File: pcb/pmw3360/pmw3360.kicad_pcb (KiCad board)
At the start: 2 copper layers, 25 x 30 mm, 20 parts, among them J1 Connector, J2 PinOut, U1 PMW3360DM-T2QU, U2 TCR2EF19,LM(CT, U3 SN74LVC1T45QDCKRQ1, U4 TXB0104RUT

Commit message: change route
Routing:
- net Net-(R1-Pad1): track 28.7 -> 27.8 mm
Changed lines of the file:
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@@
   (via (at 100.9 101.3) (size 0.8) (drill 0.4) (layers F.Cu B.Cu) (net 13))
   (segment (start 101.125645 97.974355) (end 101.125645 97.949487) (width 0.25) (layer F.Cu) (net 13))
+  (segment (start 113.025 98.575) (end 115.4 96.2) (width 0.25) (layer B.Cu) (net 13))
+  (segment (start 100.9 101.3) (end 100.9 103) (width 0.25) (layer B.Cu) (net 13))
   (segment (start 100.9 103) (end 102 104.1) (width 0.25) (layer B.Cu) (net 13))
-  (segment (start 100.9 101.3) (end 100.9 103) (width 0.25) (layer B.Cu) (net 13))
-  (segment (start 115 101.7) (end 115 96.6) (width 0.25) (layer B.Cu) (net 13))
-  (segment (start 102 104.1) (end 112.6 104.1) (width 0.25) (layer B.Cu) (net 13))
-  (segment (start 115 96.6) (end 115.4 96.2) (width 0.25) (layer B.Cu) (net 13))
-  (segment (start 112.6 104.1) (end 115 101.7) (width 0.25) (layer B.Cu) (net 13))
+  (segment (start 102 104.1) (end 111 104.1) (width 0.25) (layer B.Cu) (net 13))
+  (segment (start 111 104.1) (end 113.025 102.075) (width 0.25) (layer B.Cu) (net 13))
+  (segment (start 113.025 102.075) (end 113.025 98.575) (width 0.25) (layer B.Cu) (net 13))
   (segment (start 99.6 85.2) (end 99.6 92.863842) (width 0.25) (layer F.Cu) (net 14))
   (segment (start 99.6 92.863842) (end 101.125645 94.389487) (width 0.25) (layer F.Cu) (net 14))

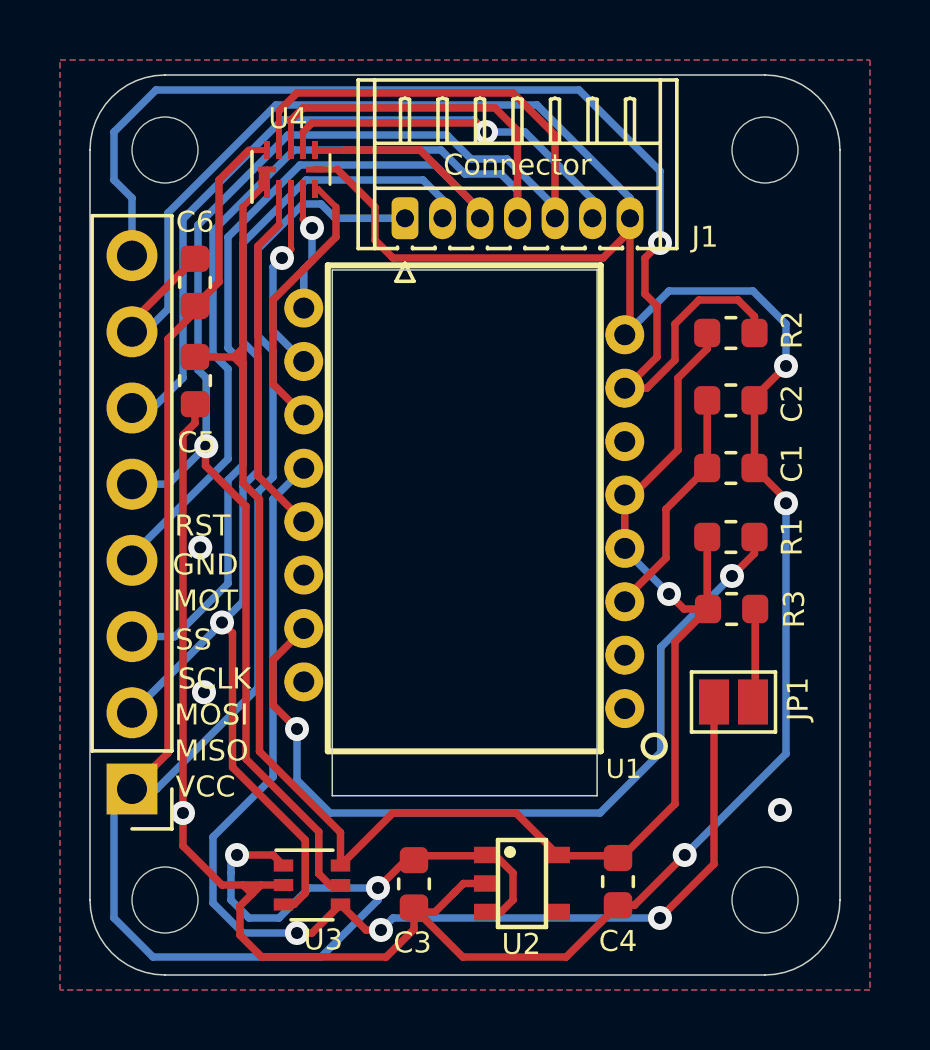
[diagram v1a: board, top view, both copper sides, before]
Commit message: change footprints position
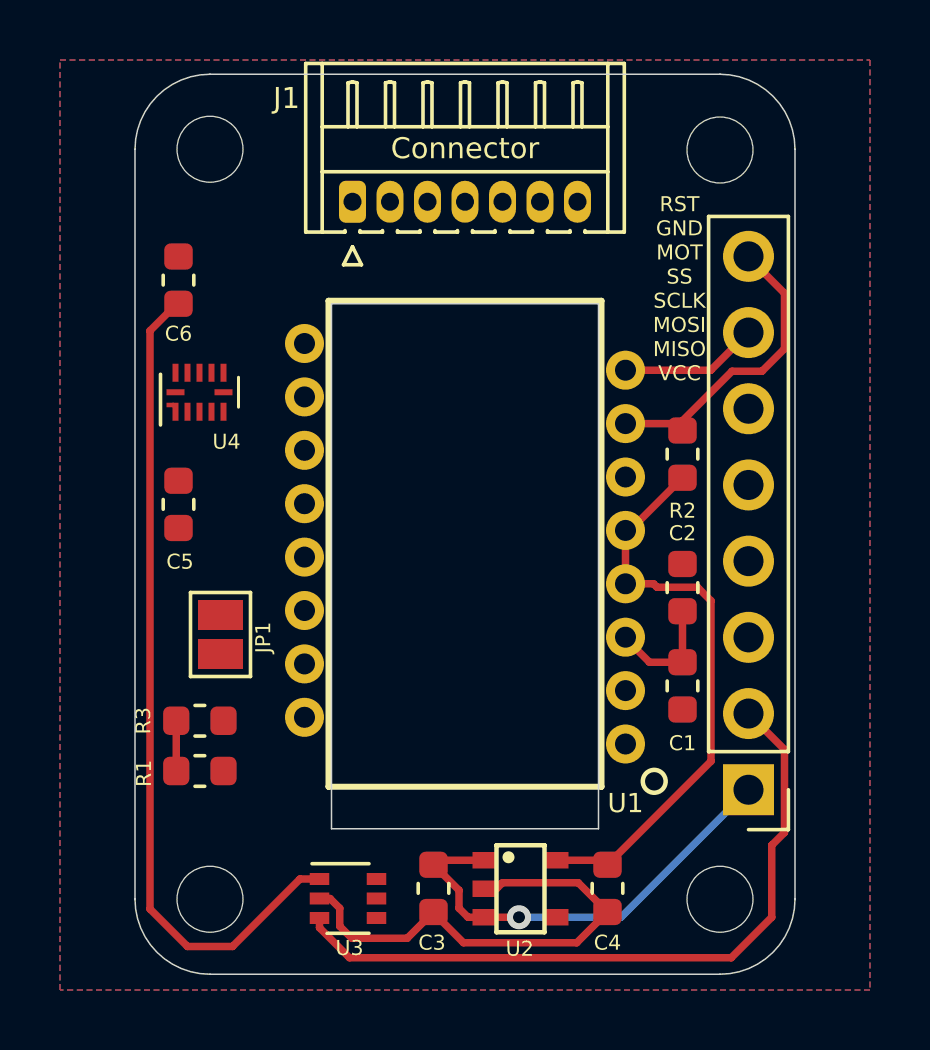
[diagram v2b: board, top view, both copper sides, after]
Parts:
- removed the REF** at (116.5, 107.0)
- removed the REF** at (96.5, 82.0)
- removed the REF** at (116.5, 82.0)
- added REF**: MountingHole_2.2mm_M2, MountingHole:MountingHole_2.2mm_M2, F.Cu at (115.0, 107.0)
- added REF**: MountingHole_2.2mm_M2, MountingHole:MountingHole_2.2mm_M2, F.Cu at (98.0, 82.0)
- added REF**: MountingHole_2.2mm_M2, MountingHole:MountingHole_2.2mm_M2, F.Cu at (115.0, 82.0)
- moved J2 20.6 mm to (116.0, 103.3)
- moved R1 19.3 mm to (97.7, 102.7)
- moved R3 18.1 mm to (97.7, 101.0)
- moved JP1 17.2 mm to (98.3, 98.2), turned to 270 degrees
- moved U4 8.03 mm to (97.7, 90.1)
- moved C1 7.44 mm to (113.8, 99.9), turned to 270 degrees
- moved C2 6.45 mm to (113.8, 96.6), turned to 90 degrees
- moved R2 4.35 mm to (113.8, 92.1), turned to 90 degrees
- moved C5 4.16 mm to (97.0, 93.8)
- moved J1 1.83 mm to (102.8, 83.7)
- moved REF** 1.50 mm to (98.0, 107.0)
- moved U3 1.28 mm to (102.6, 107.0)
- moved U1 1.18 mm to (106.5, 95.1)
- moved C3 0.67 mm to (105.5, 106.6)
- moved C6 0.56 mm to (97.0, 86.3)
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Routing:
- net GND: track 113.3 -> 20.9 mm, vias 7 -> 0
- net /SS-H: track 56.5 -> 0.00 mm, vias 1 -> 0
- net VDD: track 62.8 -> 21.2 mm, vias 1 -> 0
- net /MISO: track 39.9 -> 0.00 mm, vias 3 -> 0
- net VCC: track 81.0 -> 42.8 mm, vias 2 -> 1
- net /SCLK-H: track 37.2 -> 0.00 mm
- net /MOSI-H: track 32.8 -> 0.00 mm
- net /MOT-H: track 31.1 -> 0.00 mm, vias 1 -> 0
- net /NRESET: track 39.4 -> 10.3 mm, vias 1 -> 0
- net Net-(R1-Pad1): track 27.8 -> 0.00 mm, vias 2 -> 0
- net /MISO-H: track 37.1 -> 23.8 mm, vias 1 -> 0
- net /SS: track 12.0 -> 0.00 mm
- net /MOSI: track 9.17 -> 0.00 mm
- net /SCLK: track 6.42 -> 0.00 mm, vias 1 -> 0
- net /MOT: track 4.21 -> 0.00 mm, vias 1 -> 0
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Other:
- board size 25 x 30 mm -> 22 x 30 mm
- board text added: "RST GND MOT SS SCLK MOSI MISO VCC"
- board text removed: "GND"
- board text removed: "MISO"
- board text removed: "MOSI"
- board text removed: "MOT"
- board text removed: "RST"
- board text removed: "SCLK"
- board text removed: "SS"
- board text removed: "VCC"

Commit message: Change U3 position
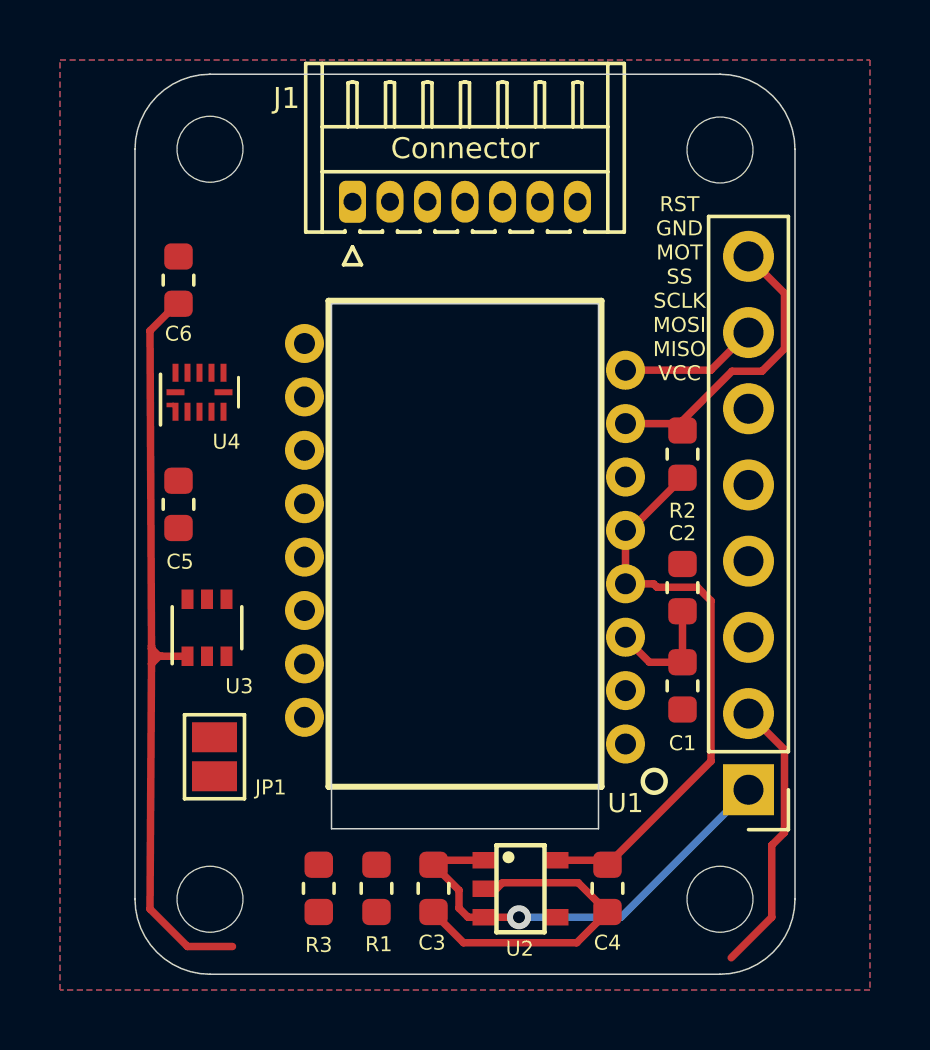
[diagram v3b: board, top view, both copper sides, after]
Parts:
- moved U3 10.2 mm to (97.9, 97.9), turned to 90 degrees
- moved R1 7.07 mm to (103.5, 106.6), turned to 270 degrees
- moved R3 6.85 mm to (101.6, 106.6), turned to 90 degrees
- moved JP1 4.08 mm to (98.2, 102.2)
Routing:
- net /MISO-H: track 23.8 -> 9.37 mm
- net GND: track 20.9 -> 15.9 mm
- net VCC: track 42.8 -> 40.7 mm
- net VDD: track 21.2 -> 19.5 mm
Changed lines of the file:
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@@
     (thickness 1.6)
     (drawings 15)
-    (tracks 66)
+    (tracks 61)
     (zones 0)
     (modules 20)
@@
   )
   (module Resistor_SMD:R_0603_1608Metric (layer F.Cu)
-    (at 97.6625 102.7 180)
+    (at 103.55 106.6125 270)
     (descr "Resistor SMD 0603 (1608 Metric), square (rectangular) end terminal, IPC_7351 nominal, (Body size source: http://www.tortai-tech.com/upload/download/2011102023233369053.pdf), generated with kicad-footprint-generator")
     (tags resistor)
     (attr smd)
-    (fp_text reference R1 (at 1.8625 -0.075 90) (layer F.SilkS)
-      (effects (font (size 0.5 0.5) (thickness 0.1)))
-    )
-    (fp_text value 39R (at -1.8375 0.025 90) (layer F.Fab)
-      (effects (font (size 0.5 0.5) (thickness 0.1)))
-    )
-    (fp_text user %R (at 0 0) (layer F.Fab)
+    (fp_text reference R1 (at 1.8625 -0.075) (layer F.SilkS)
+      (effects (font (size 0.5 0.5) (thickness 0.1)))
+    )
+    (fp_text value 39R (at 2.4875 -0.05) (layer F.Fab)
+      (effects (font (size 0.5 0.5) (thickness 0.1)))
+    )
+    (fp_text user %R (at 0 0 90) (layer F.Fab)
       (effects (font (size 0.4 0.4) (thickness 0.06)))
     )
@@
     (fp_line (start -0.8 -0.4) (end 0.8 -0.4) (layer F.Fab) (width 0.1))
     (fp_line (start -0.8 0.4) (end -0.8 -0.4) (layer F.Fab) (width 0.1))
-    (pad 2 smd roundrect (at 0.7875 0 180) (size 0.875 0.95) (layers F.Cu F.Paste F.Mask) (roundrect_rratio 0.25)
-      (net 4 VDD))
-    (pad 1 smd roundrect (at -0.7875 0 180) (size 0.875 0.95) (layers F.Cu F.Paste F.Mask) (roundrect_rratio 0.25)
+    (pad 2 smd roundrect (at 0.7875 0 270) (size 0.875 0.95) (layers F.Cu F.Paste F.Mask) (roundrect_rratio 0.25)
+      (net 4 VDD))
+    (pad 1 smd roundrect (at -0.7875 0 270) (size 0.875 0.95) (layers F.Cu F.Paste F.Mask) (roundrect_rratio 0.25)
       (net 13 "Net-(R1-Pad1)"))
     (model ${KISYS3DMOD}/Resistor_SMD.3dshapes/R_0603_1608Metric.wrl
@@
   )
   (module Resistor_SMD:R_0603_1608Metric (layer F.Cu)
-    (at 97.6625 101.025)
+    (at 101.625 106.6125 90)
     (descr "Resistor SMD 0603 (1608 Metric), square (rectangular) end terminal, IPC_7351 nominal, (Body size source: http://www.tortai-tech.com/upload/download/2011102023233369053.pdf), generated with kicad-footprint-generator")
     (tags resistor)
     (attr smd)
-    (fp_text reference R3 (at -1.8875 0 90) (layer F.SilkS)
-      (effects (font (size 0.5 0.5) (thickness 0.1)))
-    )
-    (fp_text value 10k (at 1.8125 0 90) (layer F.Fab)
-      (effects (font (size 0.5 0.5) (thickness 0.1)))
-    )
-    (fp_text user %R (at 0 0) (layer F.Fab)
+    (fp_text reference R3 (at -1.8875 0) (layer F.SilkS)
+      (effects (font (size 0.5 0.5) (thickness 0.1)))
+    )
+    (fp_text value 10k (at -2.5375 0) (layer F.Fab)
+      (effects (font (size 0.5 0.5) (thickness 0.1)))
+    )
+    (fp_text user %R (at 0 0 90) (layer F.Fab)
       (effects (font (size 0.4 0.4) (thickness 0.06)))
     )
@@
     (fp_line (start -0.8 -0.4) (end 0.8 -0.4) (layer F.Fab) (width 0.1))
     (fp_line (start -0.8 0.4) (end -0.8 -0.4) (layer F.Fab) (width 0.1))
-    (pad 2 smd roundrect (at 0.7875 0) (size 0.875 0.95) (layers F.Cu F.Paste F.Mask) (roundrect_rratio 0.25)
+    (pad 2 smd roundrect (at 0.7875 0 90) (size 0.875 0.95) (layers F.Cu F.Paste F.Mask) (roundrect_rratio 0.25)
       (net 12 "Net-(JP1-Pad2)"))
-    (pad 1 smd roundrect (at -0.7875 0) (size 0.875 0.95) (layers F.Cu F.Paste F.Mask) (roundrect_rratio 0.25)
+    (pad 1 smd roundrect (at -0.7875 0 90) (size 0.875 0.95) (layers F.Cu F.Paste F.Mask) (roundrect_rratio 0.25)
       (net 4 VDD))
     (model ${KISYS3DMOD}/Resistor_SMD.3dshapes/R_0603_1608Metric.wrl
@@
   )
   (module Package_TO_SOT_SMD:SOT-363_SC-70-6 (layer F.Cu)
-    (at 102.6 106.95)
+    (at 97.9 97.925 90)
     (descr "SOT-363, SC-70-6")
     (tags "SOT-363 SC-70-6")
     (attr smd)
-    (fp_text reference U3 (at 0.05 1.65) (layer F.SilkS)
-      (effects (font (size 0.5 0.5) (thickness 0.1)))
-    )
-    (fp_text value SN74LVC1T45QDCKRQ1 (at -0.15 6.625 -270) (layer F.Fab)
+    (fp_text reference U3 (at -1.95 1.075 180) (layer F.SilkS)
+      (effects (font (size 0.5 0.5) (thickness 0.1)))
+    )
+    (fp_text value SN74LVC1T45QDCKRQ1 (at -0.15 6.625) (layer F.Fab)
       (effects (font (size 0.5 0.5) (thickness 0.1)))
     )
@@
     (fp_line (start -0.7 1.16) (end 0.7 1.16) (layer F.SilkS) (width 0.12))
     (fp_line (start 0.7 -1.16) (end -1.2 -1.16) (layer F.SilkS) (width 0.12))
-    (fp_text user %R (at 0 0 -270) (layer F.Fab)
+    (fp_text user %R (at 0 0) (layer F.Fab)
       (effects (font (size 0.5 0.5) (thickness 0.075)))
     )
-    (pad 6 smd rect (at 0.95 -0.65) (size 0.65 0.4) (layers F.Cu F.Paste F.Mask)
-      (net 4 VDD))
-    (pad 4 smd rect (at 0.95 0.65) (size 0.65 0.4) (layers F.Cu F.Paste F.Mask)
+    (pad 6 smd rect (at 0.95 -0.65 90) (size 0.65 0.4) (layers F.Cu F.Paste F.Mask)
+      (net 4 VDD))
+    (pad 4 smd rect (at 0.95 0.65 90) (size 0.65 0.4) (layers F.Cu F.Paste F.Mask)
       (net 11 /MISO))
-    (pad 2 smd rect (at -0.95 0) (size 0.65 0.4) (layers F.Cu F.Paste F.Mask)
-      (net 1 GND))
-    (pad 5 smd rect (at 0.95 0) (size 0.65 0.4) (layers F.Cu F.Paste F.Mask)
+    (pad 2 smd rect (at -0.95 0 90) (size 0.65 0.4) (layers F.Cu F.Paste F.Mask)
+      (net 1 GND))
+    (pad 5 smd rect (at 0.95 0 90) (size 0.65 0.4) (layers F.Cu F.Paste F.Mask)
       (net 6 /SS-H))
-    (pad 3 smd rect (at -0.95 0.65) (size 0.65 0.4) (layers F.Cu F.Paste F.Mask)
+    (pad 3 smd rect (at -0.95 0.65 90) (size 0.65 0.4) (layers F.Cu F.Paste F.Mask)
       (net 9 /MISO-H))
-    (pad 1 smd rect (at -0.95 -0.65) (size 0.65 0.4) (layers F.Cu F.Paste F.Mask)
+    (pad 1 smd rect (at -0.95 -0.65 90) (size 0.65 0.4) (layers F.Cu F.Paste F.Mask)
       (net 3 VCC))
     (model ${KISYS3DMOD}/Package_TO_SOT_SMD.3dshapes/SOT-363_SC-70-6.wrl
@@
   )
   (module Jumper:SolderJumper-2_P1.3mm_Open_Pad1.0x1.5mm (layer F.Cu)
-    (at 98.35 98.15 270)
+    (at 98.15 102.225 270)
     (descr "SMD Solder Jumper, 1x1.5mm Pads, 0.3mm gap, open")
     (tags "solder jumper open")
     (attr virtual)
-    (fp_text reference JP1 (at 0.1 -1.425 90) (layer F.SilkS)
-      (effects (font (size 0.5 0.5) (thickness 0.1)))
-    )
-    (fp_text value JP_Open (at 5.725 -0.2 90) (layer F.Fab)
+    (fp_text reference JP1 (at 1.025 -1.875 180) (layer F.SilkS)
+      (effects (font (size 0.5 0.5) (thickness 0.1)))
+    )
+    (fp_text value JP_Open (at -1.375 15.45 90) (layer F.Fab)
       (effects (font (size 1 1) (thickness 0.15)))
     )
@@
   (segment (start 106.45 108.425) (end 110.225 108.425) (width 0.25) (layer F.Cu) (net 1))
   (segment (start 105.45 107.425) (end 106.45 108.425) (width 0.25) (layer F.Cu) (net 1))
-  (segment (start 104.575 108.275) (end 105.45 107.4) (width 0.25) (layer F.Cu) (net 1))
-  (segment (start 101.65 106.95) (end 102 106.95) (width 0.25) (layer F.Cu) (net 1))
-  (segment (start 102 106.95) (end 102.325 107.275) (width 0.25) (layer F.Cu) (net 1))
-  (segment (start 102.325 107.875) (end 102.725 108.275) (width 0.25) (layer F.Cu) (net 1))
-  (segment (start 102.325 107.275) (end 102.325 107.875) (width 0.25) (layer F.Cu) (net 1))
-  (segment (start 102.725 108.275) (end 104.575 108.275) (width 0.25) (layer F.Cu) (net 1))
   (segment (start 111.85 98.24) (end 111.85 98.275) (width 0.25) (layer F.Cu) (net 2))
   (segment (start 112.65 99.075) (end 113.75 99.075) (width 0.25) (layer F.Cu) (net 2))
@@
   (segment (start 111.7 107.575) (end 115.95 103.325) (width 0.25) (layer B.Cu) (net 3))
   (segment (start 108.3 107.575) (end 111.7 107.575) (width 0.25) (layer B.Cu) (net 3))
-  (segment (start 101 106.3) (end 101.65 106.3) (width 0.25) (layer F.Cu) (net 3))
-  (segment (start 98.75 108.55) (end 101 106.3) (width 0.25) (layer F.Cu) (net 3))
   (segment (start 96.95 87.125) (end 96.9 87.125) (width 0.25) (layer F.Cu) (net 3))
-  (segment (start 96 88.025) (end 96 107.3) (width 0.25) (layer F.Cu) (net 3))
   (segment (start 97.25 108.55) (end 98.75 108.55) (width 0.25) (layer F.Cu) (net 3))
   (segment (start 96.9 87.125) (end 96 88.025) (width 0.25) (layer F.Cu) (net 3))
   (segment (start 96 107.3) (end 97.25 108.55) (width 0.25) (layer F.Cu) (net 3))
+  (segment (start 96 88.025) (end 96.05 98.525) (width 0.25) (layer F.Cu) (net 3))
+  (segment (start 97.25 98.875) (end 96.4 98.875) (width 0.25) (layer F.Cu) (net 3))
+  (segment (start 96.4 98.875) (end 96.3 98.875) (width 0.25) (layer F.Cu) (net 3))
+  (segment (start 96.05 98.525) (end 96.05 99.125) (width 0.25) (layer F.Cu) (net 3))
+  (segment (start 96.3 98.875) (end 96.05 99.125) (width 0.25) (layer F.Cu) (net 3))
+  (segment (start 96.05 99.125) (end 96 107.3) (width 0.25) (layer F.Cu) (net 3))
+  (segment (start 96.05 98.625) (end 96.05 98.525) (width 0.25) (layer F.Cu) (net 3))
+  (segment (start 96.3 98.875) (end 96.05 98.625) (width 0.25) (layer F.Cu) (net 3))
   (segment (start 111.85 94.68) (end 111.85 96.46) (width 0.25) (layer F.Cu) (net 4))
   (segment (start 111.995 94.68) (end 113.75 92.925) (width 0.25) (layer F.Cu) (net 4))
@@
   (segment (start 111.1 105.675) (end 111.25 105.825) (width 0.25) (layer F.Cu) (net 4))
   (segment (start 109.55 105.675) (end 111.1 105.675) (width 0.25) (layer F.Cu) (net 4))
-  (segment (start 96.875 101.025) (end 96.875 102.7) (width 0.25) (layer F.Cu) (net 4))
-  (segment (start 101.65 107.6) (end 101.65 107.925) (width 0.25) (layer F.Cu) (net 9))
-  (segment (start 101.65 107.925) (end 102.65 108.925) (width 0.25) (layer F.Cu) (net 9))
-  (segment (start 102.65 108.925) (end 115.375 108.925) (width 0.25) (layer F.Cu) (net 9))
   (segment (start 115.375 108.925) (end 116.725 107.575) (width 0.25) (layer F.Cu) (net 9))
   (segment (start 116.725 107.575) (end 116.725 105.175) (width 0.25) (layer F.Cu) (net 9))

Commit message: routing
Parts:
- moved JP1 1.27 mm to (99.0, 103.2), turned to 180 degrees
- moved R2 0.50 mm to (113.8, 91.6)
- moved C1 0.25 mm to (113.8, 100.1)
- moved C2 0.20 mm to (113.8, 96.4)
- moved C5 0.18 mm to (96.8, 93.7)
- moved C6 0.14 mm to (96.8, 86.4)
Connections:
- U4 pad 10: /SS-H -> /MOT-H
- U4 pad 2: /SS -> /MOT
- U4 pad 3: /SCLK -> /SS
- U4 pad 4: /MOT -> /SCLK
- U4 pad 8: /MOT-H -> /SCLK-H
- U4 pad 9: /SCLK-H -> /SS-H
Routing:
- net GND: track 15.9 -> 108.5 mm, vias 0 -> 4
- net /SS-H: track 0.00 -> 57.2 mm, vias 0 -> 1
- net /MISO-H: track 9.37 -> 51.7 mm, vias 0 -> 1
- net /MOT-H: track 0.00 -> 34.0 mm
- net /SCLK-H: track 0.00 -> 34.0 mm
- net /MOSI-H: track 0.00 -> 31.9 mm
- net VDD: track 19.5 -> 50.0 mm, vias 0 -> 2
- net VCC: track 40.7 -> 56.3 mm, vias 1 -> 2
- net /MISO: track 0.00 -> 12.0 mm
- net Net-(R1-Pad1): track 0.00 -> 9.04 mm
- net /MOT: track 0.00 -> 8.09 mm, vias 0 -> 1
- net Net-(JP1-Pad2): track 0.00 -> 6.78 mm
- net /SS: track 0.00 -> 6.62 mm, vias 0 -> 1
- net /SCLK: track 0.00 -> 4.54 mm, vias 0 -> 1
- net /MOSI: track 0.00 -> 3.23 mm
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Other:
- board text added: "GND"
- board text added: "MISO"
- board text added: "MOSI"
- board text added: "MOT"
- board text added: "RST"
- board text added: "SCLK"
- board text added: "SS"
- board text added: "VCC"
